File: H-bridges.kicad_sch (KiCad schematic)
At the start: 38 parts, among them J2 Conn_Coaxial, J3 Conn_Coaxial, J6 Conn_Coaxial, J7 Conn_Coaxial, Q10 NMOS, Q11 NMOS, Q12 NMOS, Q13 NMOS, Q14 NMOS, Q7 NMOS, Q8 NMOS, Q9 NMOS, U10 MIC4604YM, U11 MIC4604YM, U8 MIC4604YM, U9 MIC4604YM

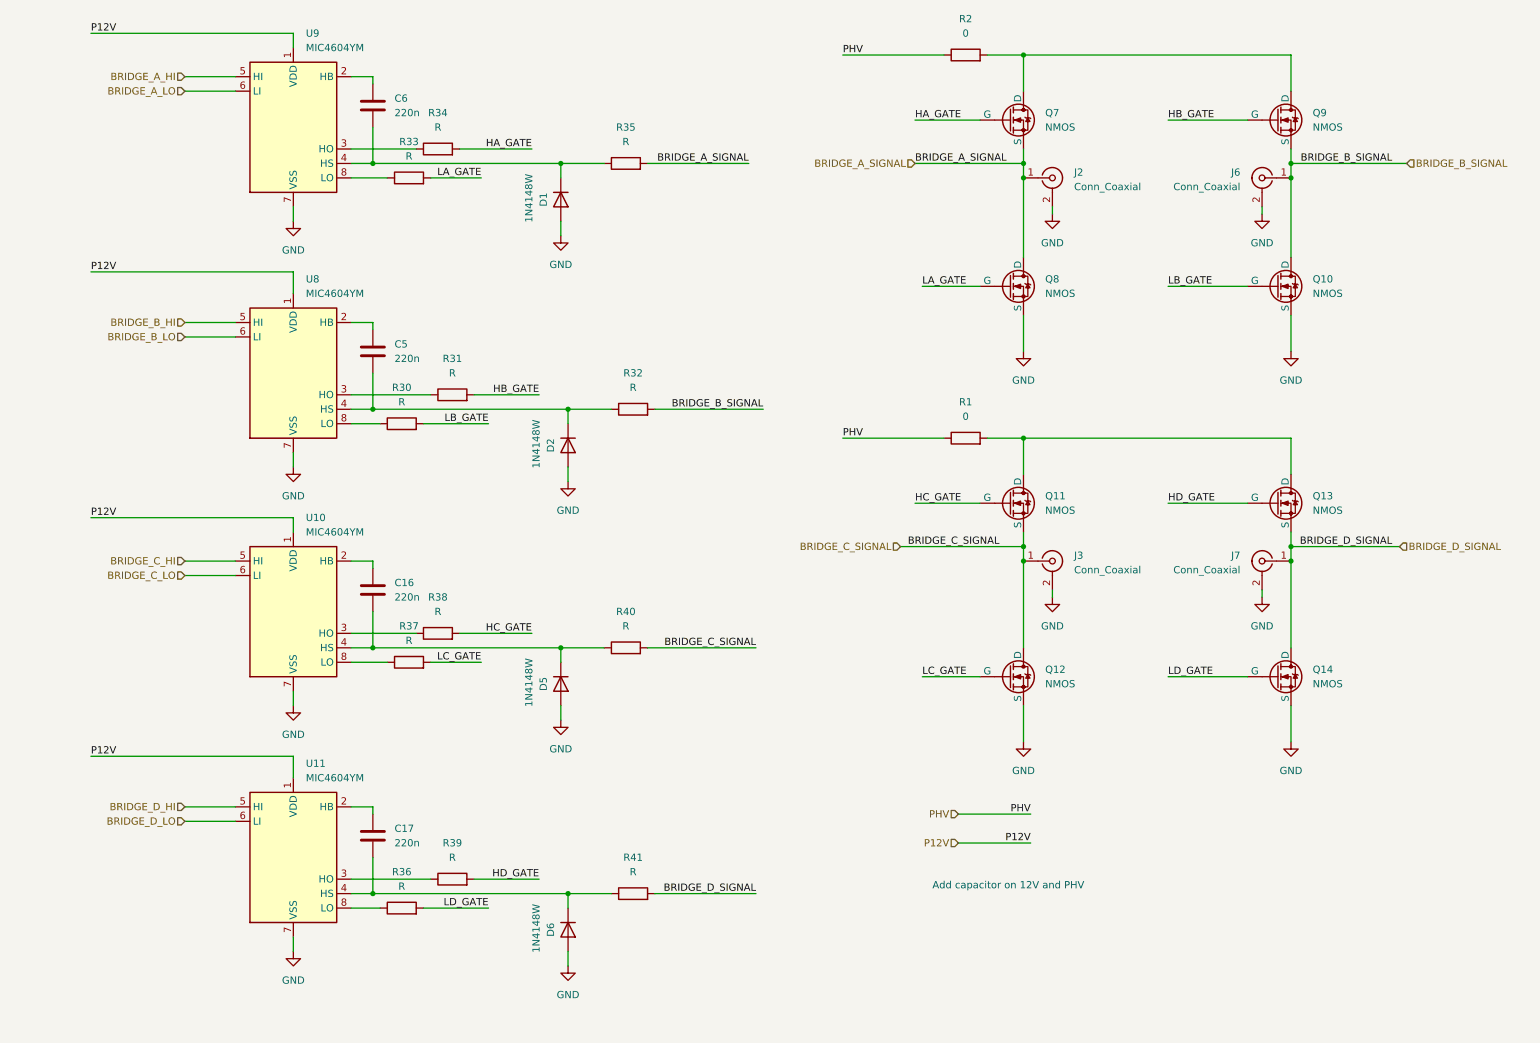
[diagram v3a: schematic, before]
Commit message: schematic ready, basic layout done
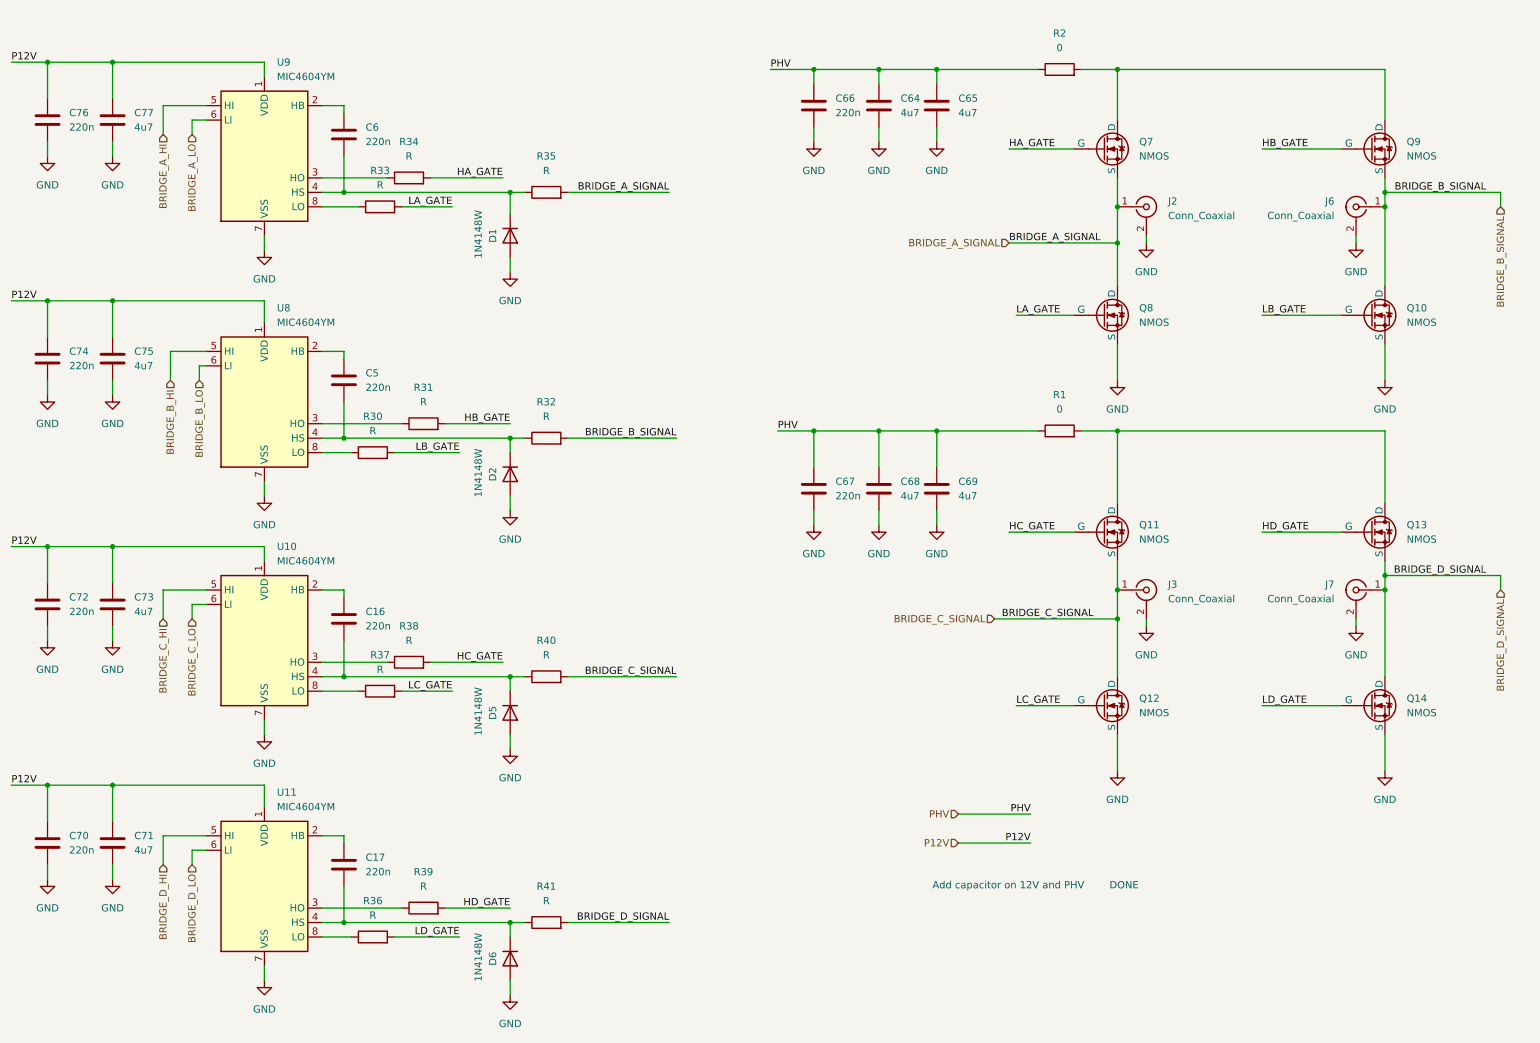
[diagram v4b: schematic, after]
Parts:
- added C64, C65, C68, C69, C71, C73, C75, C77: 4u7, Capacitor_SMD:C_0805_2012Metric_Pad1.18x1.45mm_HandSolder, symbol Device:C
- added C66, C67, C70, C72, C74, C76: 220n, Capacitor_SMD:C_0603_1608Metric_Pad1.08x0.95mm_HandSolder, symbol Device:C
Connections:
- net GND: now also C64.1, C65.1, C66.2, C67.2, C68.1, C69.1, C70.2, C71.1, C72.2, C73.1, C74.2, C75.1, C76.2, C77.1
- net P12V: now also C70.1, C71.2, C72.1, C73.2, C74.1, C75.2, C76.1, C77.2
- net PHV: now also C64.2, C65.2, C66.1, C67.1, C68.2, C69.2
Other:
- note added: "Add capacitor on 12V and PHV DONE"
- note removed: "Add capacitor on 12V and PHV"
- moved on the sheet: C16, C17, C5, C6, D1, D2, D5, D6, J2, J3, J6, J7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

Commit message: before changing MUX
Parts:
- added U19: ~, Package_SO:VSSOP-8_3.0x3.0mm_P0.65mm, symbol 10_ICs:TMUX7219
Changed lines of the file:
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@@
 	)
 	(symbol
+		(lib_id "10_ICs:TMUX7219")
+		(at 166.37 53.34 0)
+		(mirror y)
+		(unit 1)
+		(exclude_from_sim no)
+		(in_bom yes)
+		(on_board yes)
+		(dnp no)
+		(fields_autoplaced yes)
+		(property "Reference" "U19"
+			(at 161.29 49.53 0)
+			(effects
+				(font
+					(size 1.27 1.27)
+				)
+			)
+		)
+		(property "Value" "~"
+			(at 161.29 52.07 0)
+			(effects
+				(font
+					(size 1.27 1.27)
+				)
+			)
+		)
+		(property "Footprint" "Package_SO:VSSOP-8_3.0x3.0mm_P0.65mm"
+			(at 166.37 53.34 0)
+			(effects
+				(font
+					(size 1.27 1.27)
+				)
+				(hide yes)
+			)
+		)
+		(property "Datasheet" ""
+			(at 166.37 53.34 0)
+			(effects
+				(font
+					(size 1.27 1.27)
+				)
+				(hide yes)
+			)
+		)
+		(property "Description" ""
+			(at 166.37 53.34 0)
+			(effects
+				(font
+					(size 1.27 1.27)
+				)
+				(hide yes)
+			)
+		)
+		(pin "2"
+		)
+		(pin "6"
+		)
+		(pin "5"
+		)
+		(pin "7"
+		)
+		(pin "8"
+		)
+		(pin "1"
+		)
+		(pin "3"
+		)
+		(pin "4"
+		)
+		(instances
+			(project "ultrasonic_V3_HW"
+				(path "/731d4032-cf8d-4f76-95ca-2ec44c8e0816/ae9acf88-c042-4005-997d-04f4c43f38c7"
+					(reference "U19")
+					(unit 1)
+				)
+			)
+		)
+	)
+	(symbol
 		(lib_id "Device:C")
 		(at 34.29 34.29 180)
@@
 				)
 			)
+		)
+	)
+	(symbol
+		(lib_id "10_ICs:TMUX7219")
+		(at 168.91 177.8 0)
+		(mirror y)
+		(unit 2)
+		(exclude_from_sim no)
+		(in_bom yes)
+		(on_board yes)
+		(dnp no)
+		(fields_autoplaced yes)
+		(property "Reference" "U19"
+			(at 163.83 173.99 0)
+			(effects
+				(font
+					(size 1.27 1.27)
+				)
+			)
+		)
+		(property "Value" "~"
+			(at 163.83 176.53 0)
+			(effects
+				(font
+					(size 1.27 1.27)
+				)
+			)
+		)
+		(property "Footprint" "Package_SO:VSSOP-8_3.0x3.0mm_P0.65mm"
+			(at 168.91 177.8 0)
+			(effects
+				(font
+					(size 1.27 1.27)
+				)
+				(hide yes)
+			)
+		)
+		(property "Datasheet" ""
+			(at 168.91 177.8 0)
+			(effects
+				(font
+					(size 1.27 1.27)
+				)
+				(hide yes)
+			)
+		)
+		(property "Description" ""
+			(at 168.91 177.8 0)
+			(effects
+				(font
+					(size 1.27 1.27)
+				)
+				(hide yes)
+			)
+		)
+		(pin "2"
+		)
+		(pin "6"
+		)
+		(pin "5"
+		)
+		(pin "7"
+		)
+		(pin "8"
+		)
+		(pin "1"
+		)
+		(pin "3"
+		)
+		(pin "4"
+		)
+		(instances
+			(project "ultrasonic_V3_HW"
+				(path "/731d4032-cf8d-4f76-95ca-2ec44c8e0816/ae9acf88-c042-4005-997d-04f4c43f38c7"
+					(reference "U19")
+					(unit 2)
+				)
+			)

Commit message: no errors schematic, basic routing done
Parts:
- removed Q10, Q11, Q12, Q13, Q14, Q7, Q8, Q9: NMOS, Package_TO_SOT_SMD:SOT-223-3_TabPin2, symbol Simulation_SPICE:NMOS
- added C81, C82, C83, C84, C86, C87: C, Capacitor_SMD:C_0603_1608Metric_Pad1.08x0.95mm_HandSolder, symbol Device:C
- added Q1, Q10, Q2, Q3, Q4, Q7, Q8, Q9: DMN6069SE, Package_TO_SOT_SMD:SOT-223-3_TabPin2, symbol 10_ICs:DMN6069SE
- added R10, R9: R, Resistor_SMD:R_1206_3216Metric_Pad1.30x1.75mm_HandSolder, symbol Device:R
- added U20, U21, U22: TMUX7219, Package_SO:VSSOP-8_3.0x3.0mm_P0.65mm, symbol 10_ICs:TMUX7219
- C16, C17, C5, C6, C66, C67, C70, C72, C74, C76: value 220n -> C
- C64, C65, C68, C69, C71, C73, C75, C77: value 4u7 -> C
- D1, D2, D5, D6: value 1N4148W -> D
- R1, R2: value 0 -> R
- U19: value ~ -> TMUX7219
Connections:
- net GND: now also U19.3 (GND), U19.7 (VSS), C81.2, C82.2, C83.2, C84.2, C86.2, C87.2, Q1.3 (S), Q10.3 (S), Q4.3 (S), Q9.3 (S), U20.3 (GND), U20.7 (VSS), U21.3 (GND), U21.7 (VSS), U22.3 (GND), U22.7 (VSS)
- net HA_GATE: now also Q3.1 (G)
- net HB_GATE: now also Q2.1 (G)
- net HC_GATE: now also Q7.1 (G)
- net HD_GATE: now also Q8.1 (G)
- net LA_GATE: now also Q4.1 (G)
- net LB_GATE: now also Q1.1 (G)
- net LC_GATE: now also Q9.1 (G)
- net LD_GATE: now also Q10.1 (G)
- net PHV: now also R1.2, R2.2, U19.4 (VDD), C81.1, C82.1, C83.1, C84.1, C86.1, C87.1, R10.2, R9.2, U20.4 (VDD), U21.4 (VDD), U22.4 (VDD); no longer R1.1, R2.1
- net at U19.1 (D): now also J2.1 (In), Q3.3 (S), Q4.2 (D)
- net BRIDGE_A_MIDDLE: now reaches U19.2 (S1)
- net BRIDGE_A_MIDDLE: now also R35.2
- net BRIDGE_AB_MUX_EN: now reaches U19.5 (EN)
- net BRIDGE_AB_MUX_EN: now also U22.5 (EN)
- net BRIDGE_A_SEL: now reaches U19.6 (SEL)
- net SIGNAL_UNAMPLIFIED_P: now reaches U19.8 (S2)
- net SIGNAL_UNAMPLIFIED_P: now also U20.8 (S2)
- removed net BRIDGE_A_SIGNAL: J2.1 (In), R35.2
- net BRIDGE_B_SIGNAL: no longer names the net of J6.1 (In)
- net BRIDGE_B_SIGNAL: now also Q1.2 (D), Q2.3 (S), U22.1 (D); no longer R32.2
- net BRIDGE_C_SIGNAL: no longer names the net of J3.1 (In)
- net BRIDGE_C_SIGNAL: now also Q7.3 (S), Q9.2 (D), U20.1 (D); no longer R40.2
- net BRIDGE_D_SIGNAL: no longer names the net of J7.1 (In)
- net BRIDGE_D_SIGNAL: now also Q10.2 (D), Q8.3 (S), U21.1 (D); no longer R41.2
- new net: Q2.2 (D), R9.1
- new net: Q7.2 (D), R1.1
- new net: Q8.2 (D), R10.1
- new net: Q3.2 (D), R2.1
- new net BRIDGE_B_MIDDLE: R32.2, U22.2 (S1)
- new net BRIDGE_B_SEL: U22.6 (SEL)
- new net BRIDGE_CD_MUX_EN: U20.5 (EN), U21.5 (EN)
- new net BRIDGE_C_MIDDLE: R40.2, U20.2 (S1)
- new net BRIDGE_C_SEL: U20.6 (SEL)
- new net BRIDGE_D_MIDDLE: R41.2, U21.2 (S1)
- new net BRIDGE_D_SEL: U21.6 (SEL)
- new net SIGNAL_UNAMPLIFIED_N: U21.8 (S2), U22.8 (S2)
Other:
- moved on the sheet: C64, C65, C66, C67, C68, C69, J2, J3, J6, J7, U19A, U19B

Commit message: DONE - before checking
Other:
- note added: "Drivers"
- note added: "MOSFET and switch"
- note added: "Power pins and hierarchy"
- moved on the sheet: C16, C17, C5, C6, C67, C68, C69, C70, C71, C72, C73, C74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
